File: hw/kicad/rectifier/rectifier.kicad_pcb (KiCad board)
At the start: 2 copper layers, 93.9 x 46 mm, 21 parts, among them K1 CONN_3, P1 CONN_2, P2 CONN_2, P3 CONN_2, P4 CONN_2, P5 CONN_1

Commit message: Small changes.
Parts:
- moved REF** 0.11 mm to (58.4, 74.6)
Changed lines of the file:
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@@
   )
   (setup
-    (last_trace_width 1)
+    (last_trace_width 0.25)
     (user_trace_width 1)
     (user_trace_width 2.5)
@@
     (add_net Neutral)
     (add_net PE)
+  )
+  (module Fuse_Holders_and_Fuses:Fuseholder5x20_horiz_SemiClosed_Casing10x25mm (layer F.Cu)
+    (at 53.4162 89.8017 270)
+    (descr "Fuseholder, 5x20, Semi closed, horizontal, Casing 10x25mm,")
+    (tags "Fuseholder, 5x20, Semi closed, horizontal, Casing 10x25mm, Sicherungshalter, halbgeschlossen,")
+    (fp_text reference F1 (at 0 -7.62 270) (layer F.SilkS)
+      (effects (font (size 1 1) (thickness 0.15)))
+    )
+    (fp_text value FUSE (at 1.27 7.62 270) (layer F.Fab)
+      (effects (font (size 1 1) (thickness 0.15)))
+    )
+    (fp_line (start -5.99948 -2.49936) (end -5.99948 -5.00126) (layer F.SilkS) (width 0.15))
+    (fp_line (start -5.99948 5.00126) (end -5.99948 2.49936) (layer F.SilkS) (width 0.15))
+    (fp_line (start 5.99948 5.00126) (end 5.99948 2.49936) (layer F.SilkS) (width 0.15))
+    (fp_line (start 5.99948 -5.00126) (end 5.99948 -2.49936) (layer F.SilkS) (width 0.15))
+    (fp_line (start 11.99896 -1.89992) (end 11.99896 -5.00126) (layer F.SilkS) (width 0.15))
+    (fp_line (start -11.99896 1.89992) (end -11.99896 5.00126) (layer F.SilkS) (width 0.15))
+    (fp_line (start -11.99896 5.00126) (end 11.99896 5.00126) (layer F.SilkS) (width 0.15))
+    (fp_line (start 11.99896 5.00126) (end 11.99896 1.89992) (layer F.SilkS) (width 0.15))
+    (fp_line (start 11.99896 -5.00126) (end -11.99896 -5.00126) (layer F.SilkS) (width 0.15))
+    (fp_line (start -11.99896 -5.00126) (end -11.99896 -1.89992) (layer F.SilkS) (width 0.15))
+    (pad 2 thru_hole oval (at 11.00074 0 180) (size 2.49936 4.0005) (drill 1.50114) (layers *.Cu *.Mask F.SilkS)
+      (net 8 AC_fused))
+    (pad 1 thru_hole oval (at -11.00074 0 180) (size 2.49936 4.0005) (drill 1.50114) (layers *.Cu *.Mask F.SilkS)
+      (net 9 "Net-(F1-Pad1)"))
   )
   (module Resistors_ThroughHole:Resistor_Vertical_RM7.5mm (layer F.Cu)
@@
       (net 2 DC-))
   )
-  (module Fuse_Holders_and_Fuses:Fuseholder5x20_horiz_SemiClosed_Casing10x25mm (layer F.Cu)
-    (at 53.4162 89.8017 270)
-    (descr "Fuseholder, 5x20, Semi closed, horizontal, Casing 10x25mm,")
-    (tags "Fuseholder, 5x20, Semi closed, horizontal, Casing 10x25mm, Sicherungshalter, halbgeschlossen,")
-    (fp_text reference F1 (at 0 -7.62 270) (layer F.SilkS)
-      (effects (font (size 1 1) (thickness 0.15)))
-    )
-    (fp_text value FUSE (at 1.27 7.62 270) (layer F.Fab)
-      (effects (font (size 1 1) (thickness 0.15)))
-    )
-    (fp_line (start -5.99948 -2.49936) (end -5.99948 -5.00126) (layer F.SilkS) (width 0.15))
-    (fp_line (start -5.99948 5.00126) (end -5.99948 2.49936) (layer F.SilkS) (width 0.15))
-    (fp_line (start 5.99948 5.00126) (end 5.99948 2.49936) (layer F.SilkS) (width 0.15))
-    (fp_line (start 5.99948 -5.00126) (end 5.99948 -2.49936) (layer F.SilkS) (width 0.15))
-    (fp_line (start -4.50088 0) (end 4.50088 0) (layer F.SilkS) (width 0.15))
-    (fp_line (start -4.50088 -2.49936) (end -4.50088 2.49936) (layer F.SilkS) (width 0.15))
-    (fp_line (start 4.50088 -2.49936) (end 4.50088 2.49936) (layer F.SilkS) (width 0.15))
-    (fp_line (start 9.99998 -1.89992) (end 9.99998 -2.49936) (layer F.SilkS) (width 0.15))
-    (fp_line (start -9.99998 1.89992) (end -9.99998 2.49936) (layer F.SilkS) (width 0.15))
-    (fp_line (start -9.99998 2.49936) (end 9.99998 2.49936) (layer F.SilkS) (width 0.15))
-    (fp_line (start 9.99998 2.49936) (end 9.99998 1.89992) (layer F.SilkS) (width 0.15))
-    (fp_line (start 9.99998 -2.49936) (end -9.99998 -2.49936) (layer F.SilkS) (width 0.15))
-    (fp_line (start -9.99998 -2.49936) (end -9.99998 -1.89992) (layer F.SilkS) (width 0.15))
-    (fp_line (start 11.99896 -1.89992) (end 11.99896 -5.00126) (layer F.SilkS) (width 0.15))
-    (fp_line (start -11.99896 1.89992) (end -11.99896 5.00126) (layer F.SilkS) (width 0.15))
-    (fp_line (start -11.99896 5.00126) (end 11.99896 5.00126) (layer F.SilkS) (width 0.15))
-    (fp_line (start 11.99896 5.00126) (end 11.99896 1.89992) (layer F.SilkS) (width 0.15))
-    (fp_line (start 11.99896 -5.00126) (end -11.99896 -5.00126) (layer F.SilkS) (width 0.15))
-    (fp_line (start -11.99896 -5.00126) (end -11.99896 -1.89992) (layer F.SilkS) (width 0.15))
-    (pad 2 thru_hole oval (at 11.00074 0 180) (size 2.49936 4.0005) (drill 1.50114) (layers *.Cu *.Mask F.SilkS)
-      (net 8 AC_fused))
-    (pad 1 thru_hole oval (at -11.00074 0 180) (size 2.49936 4.0005) (drill 1.50114) (layers *.Cu *.Mask F.SilkS)
-      (net 9 "Net-(F1-Pad1)"))
-  )
   (module custom_footprints:WE313-3 (layer F.Cu)
     (at 45.085 79.375 270)
@@
     (descr "Mounting hole, Befestigungsbohrung, 3mm, No Annular, Kein Restring,")
     (tags "Mounting hole, Befestigungsbohrung, 3mm, No Annular, Kein Restring,")
-    (fp_text reference REF** (at 0 -4.0005) (layer F.SilkS)
+    (fp_text reference REF** (at 0 -4.0005) (layer F.SilkS) hide
       (effects (font (size 1 1) (thickness 0.15)))
     )
@@
     (descr "Mounting hole, Befestigungsbohrung, 3mm, No Annular, Kein Restring,")
     (tags "Mounting hole, Befestigungsbohrung, 3mm, No Annular, Kein Restring,")
-    (fp_text reference REF** (at 0 -4.0005) (layer F.SilkS)
+    (fp_text reference REF** (at 0 -4.0005) (layer F.SilkS) hide
       (effects (font (size 1 1) (thickness 0.15)))
     )
@@
     (descr "Mounting hole, Befestigungsbohrung, 3mm, No Annular, Kein Restring,")
     (tags "Mounting hole, Befestigungsbohrung, 3mm, No Annular, Kein Restring,")
-    (fp_text reference REF** (at 0 -4.0005) (layer F.SilkS)
+    (fp_text reference REF** (at 0 -4.0005) (layer F.SilkS) hide
       (effects (font (size 1 1) (thickness 0.15)))
     )
@@
   )
   (module Mounting_Holes:MountingHole_3mm (layer F.Cu)
-    (at 58.547 74.676)
+    (at 58.44 74.643)
     (descr "Mounting hole, Befestigungsbohrung, 3mm, No Annular, Kein Restring,")
     (tags "Mounting hole, Befestigungsbohrung, 3mm, No Annular, Kein Restring,")
-    (fp_text reference REF** (at 0 -4.0005) (layer F.SilkS)
-      (effects (font (size 1 1) (thickness 0.15)))
-    )
+    (fp_text reference REF** (at 0 -4.0005) (layer F.SilkS) hide
+      (effects (font (size 1 1) (thickness 0.15)))
+    )

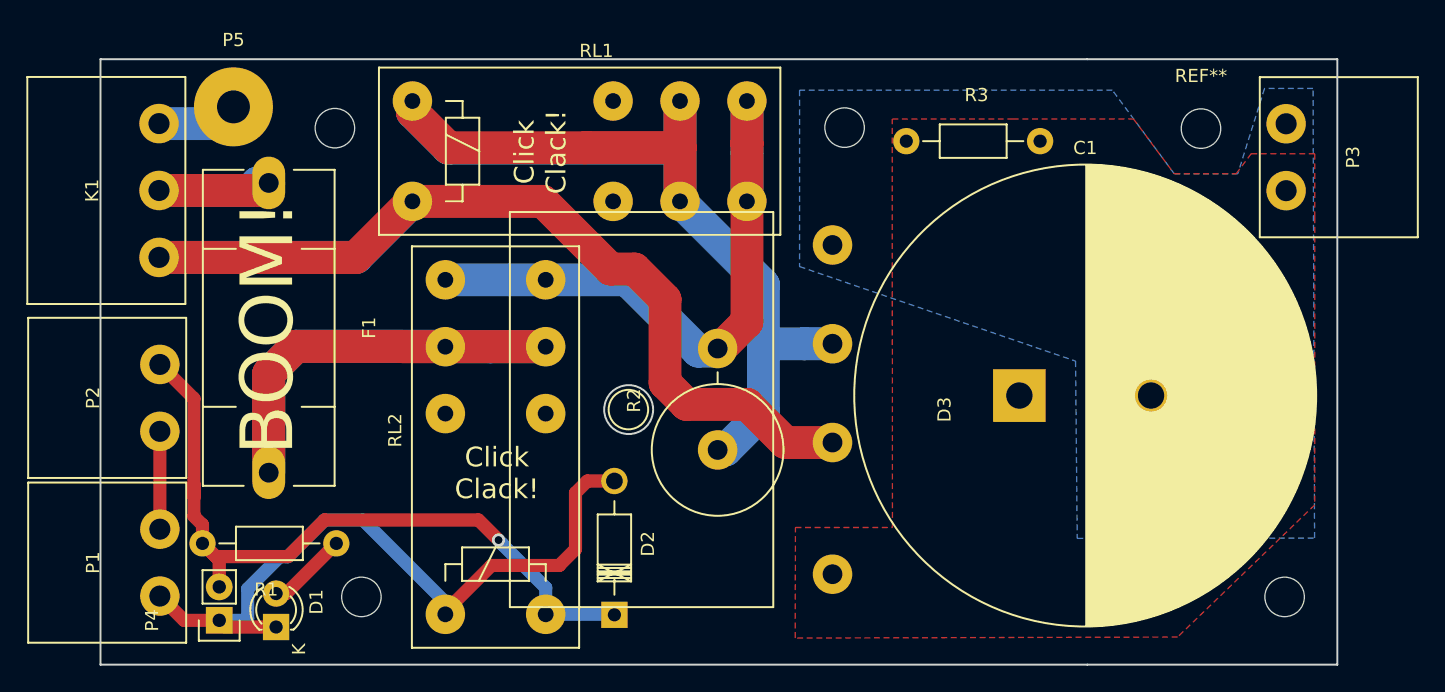
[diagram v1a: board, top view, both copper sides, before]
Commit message: Reworked rectifier for increased safety
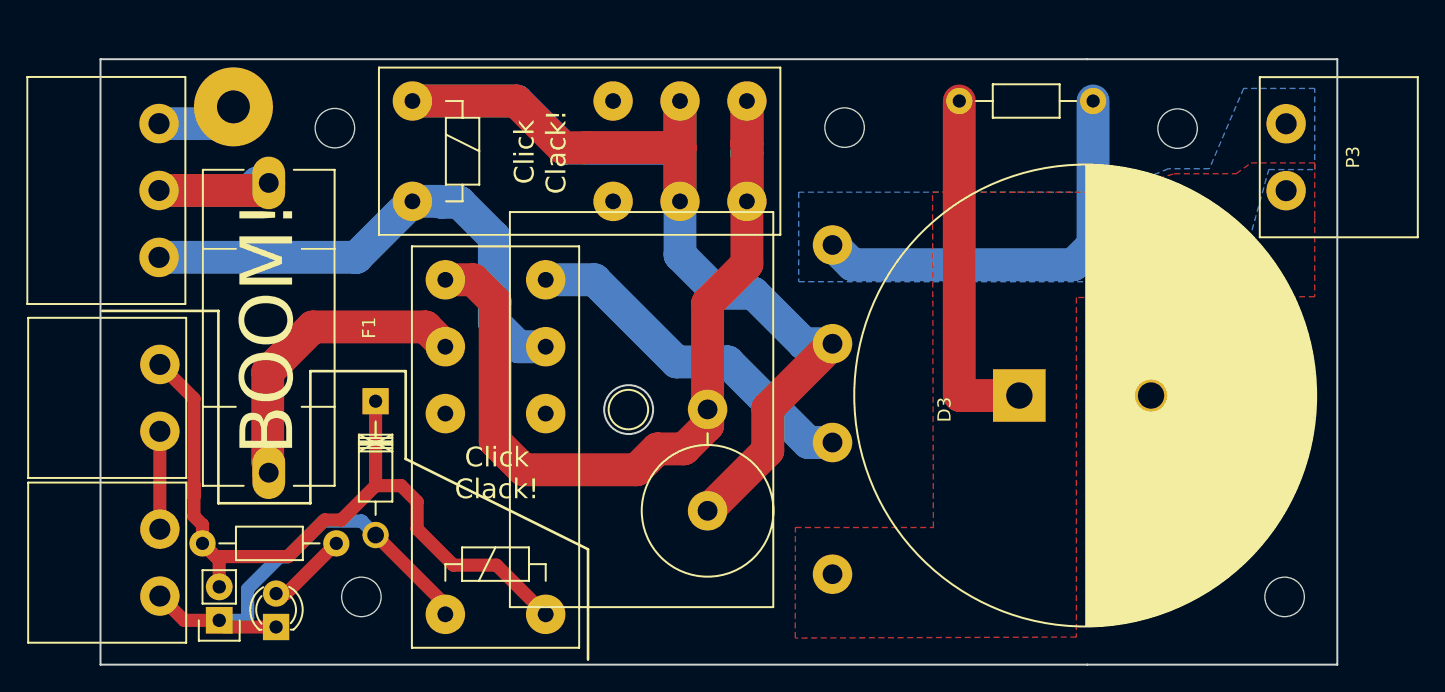
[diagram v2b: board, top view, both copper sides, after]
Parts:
- moved D2 24.3 mm to (61.5, 95.4), turned to 270 degrees
- moved R3 5.05 mm to (110.9, 72.6)
- moved R2 4.69 mm to (86.7, 99.9)
- moved REF** 1.78 mm to (122.4, 74.7)
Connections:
- D3 pad 2: Neutral -> Neutral_Switched
- RL2 pad 21: AC_fused -> Neutral
- RL2 pad 24: AC_switched -> Neutral_Switched
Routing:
- net Neutral: track 85.2 -> 39.5 mm
- net AC_fused: track 58.9 -> 23.3 mm
- net DC-: track 0.00 -> 32.0 mm
- net Neutral_Switched: track 0.00 -> 26.9 mm
- net DC+: track 0.00 -> 26.9 mm
- net Net-(D1-Pad1): track 54.8 -> 35.7 mm
- net AC_switched: track 50.5 -> 68.2 mm
- net AC_ntc: track 88.4 -> 93.9 mm
- net Net-(D2-Pad1): track 56.7 -> 60.0 mm, vias 1 -> 0
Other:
- board text added: "DANGER! May hold charge for longer than you think. It _will_ kill you dead."

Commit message: Bump version number
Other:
- board text added: "Stmbl Gleich-Riecht-Er V0.0.2"
- board text removed: "Stmbl Gleich-Riecht-Er V0.0.1"
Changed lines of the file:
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@@
-(kicad_pcb (version 4) (host pcbnew "(2016-01-09 BZR 6434, Git 5e36c48)-product")
+(kicad_pcb (version 4) (host pcbnew "(2016-01-14 BZR 6474)-product")
   (general
     (links 29)
-    (no_connects 4)
-    (area 40.564999 69.330499 134.631501 115.454501)
+    (no_connects 0)
+    (area 34.809999 66.82 140.945301 116.21226)
     (thickness 1.6)
     (drawings 30)
@@
   )
   (setup
-    (last_trace_width 1)
+    (last_trace_width 0.25)
     (user_trace_width 1)
     (user_trace_width 2.5)
@@
     (effects (font (size 1.5 1.5) (thickness 0.3)) (justify mirror))
   )
-  (gr_text "Stmbl\nGleich-Riecht-Er\nV0.0.1" (at 114.554 105.156) (layer B.SilkS)
+  (gr_text "Stmbl\nGleich-Riecht-Er\nV0.0.2" (at 114.554 105.156) (layer B.SilkS)
     (effects (font (size 1.5 1.5) (thickness 0.3)) (justify mirror))
   )
